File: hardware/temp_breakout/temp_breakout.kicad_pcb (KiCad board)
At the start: 2 copper layers, 45.5 x 48.5 mm, 14 parts, among them J1 Conn_01x04, J2 Conn_01x03, J3 Conn_01x03, J4 Conn_01x03, J5 Conn_01x03, J6 Conn_01x03, J7 Conn_01x03

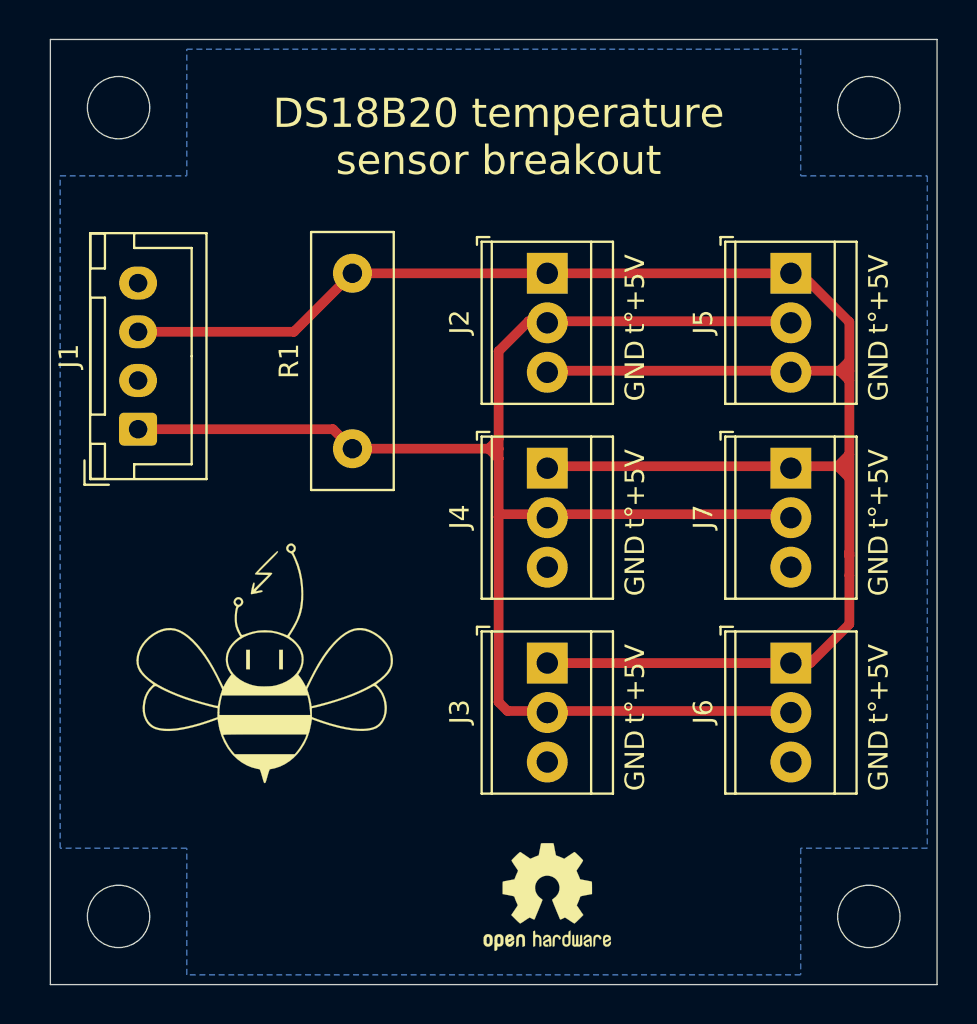
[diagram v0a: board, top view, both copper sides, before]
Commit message: fix temp breakout board bug: 5V and gnd were shorted
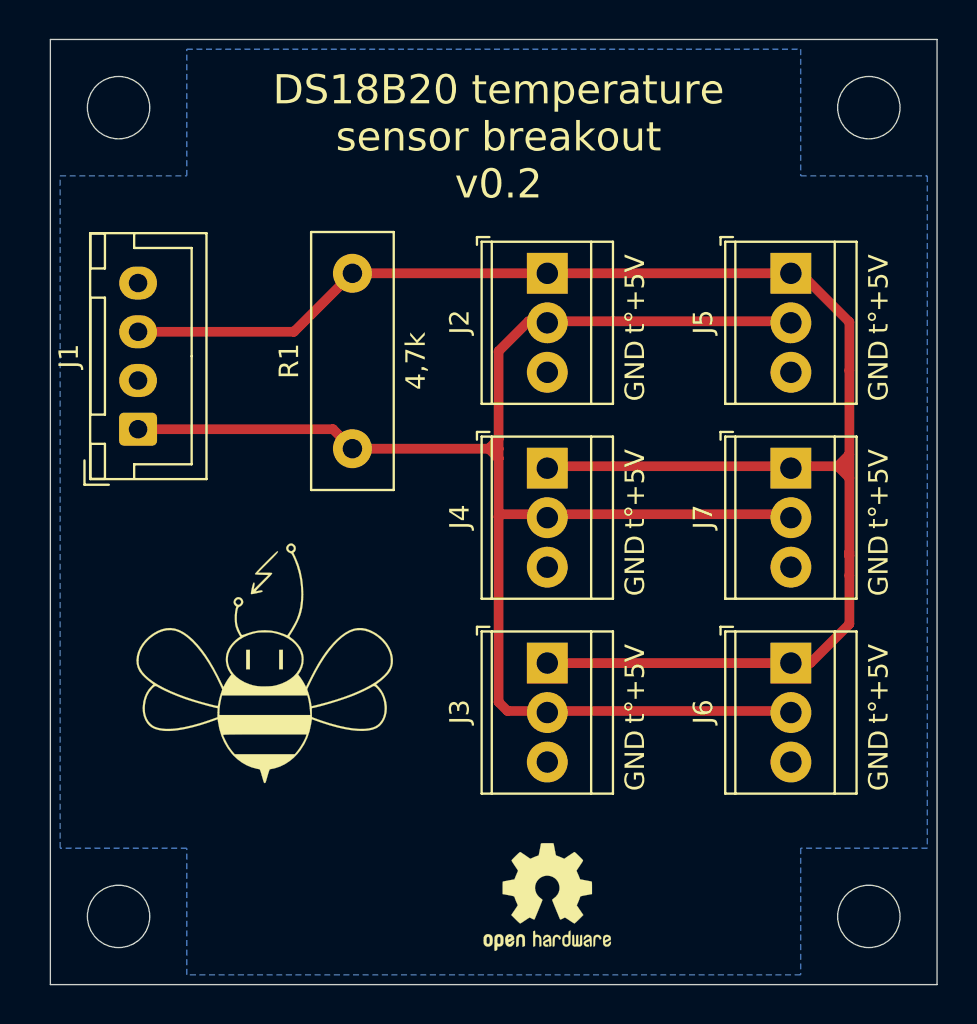
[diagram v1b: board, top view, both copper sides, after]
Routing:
- net +5V: track 104.3 -> 87.4 mm
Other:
- board text added: "DS18B20 temperature sensor breakout v0.2"
- board text removed: "DS18B20 temperature sensor breakout"
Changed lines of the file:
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@@
-(kicad_pcb (version 20171130) (host pcbnew "(5.1.7)-1")
+(kicad_pcb (version 20171130) (host pcbnew 5.1.10-88a1d61d58~90~ubuntu20.04.1)
   (general
     (thickness 1.6)
     (drawings 26)
-    (tracks 38)
+    (tracks 35)
     (zones 0)
     (modules 14)
@@
   )
   (setup
-    (last_trace_width 0.5)
+    (last_trace_width 0.25)
     (user_trace_width 0.5)
     (trace_clearance 0.2)
@@
     (visible_elements FFFFFF7F)
     (pcbplotparams
-      (layerselection 0x010fc_ffffffff)
+      (layerselection 0x3ffff_ffffffff)
       (usegerberextensions false)
       (usegerberattributes true)
@@
       (effects (font (size 1 1) (thickness 0.15)))
     )
-    (fp_text user %R (at 2.54 2 90) (layer F.Fab)
-      (effects (font (size 1 1) (thickness 0.15)))
-    )
     (fp_line (start 7.08 -3.75) (end -2 -3.75) (layer F.CrtYd) (width 0.05))
     (fp_line (start 7.08 3.75) (end 7.08 -3.75) (layer F.CrtYd) (width 0.05))
@@
     (fp_circle (center 2.54 0) (end 3.64 0) (layer F.Fab) (width 0.1))
     (fp_circle (center 0 0) (end 1.1 0) (layer F.Fab) (width 0.1))
+    (fp_text user %R (at 2.54 2 90) (layer F.Fab)
+      (effects (font (size 1 1) (thickness 0.15)))
+    )
     (pad 3 thru_hole circle (at 5.08 0 270) (size 2.1 2.1) (drill 1.1) (layers *.Cu *.Mask)
       (net 1 GND))
@@
     )
     (fp_text value Conn_01x03 (at 2.54 4.37 90) (layer F.Fab)
-      (effects (font (size 1 1) (thickness 0.15)))
-    )
-    (fp_text user %R (at 2.54 2 90) (layer F.Fab)
       (effects (font (size 1 1) (thickness 0.15)))
     )
@@
     (fp_circle (center 2.54 0) (end 3.64 0) (layer F.Fab) (width 0.1))
     (fp_circle (center 0 0) (end 1.1 0) (layer F.Fab) (width 0.1))
+    (fp_text user %R (at 2.54 2 90) (layer F.Fab)
+      (effects (font (size 1 1) (thickness 0.15)))
+    )
     (pad 3 thru_hole circle (at 5.08 0 270) (size 2.1 2.1) (drill 1.1) (layers *.Cu *.Mask)
       (net 1 GND))
@@
     )
     (fp_text value Conn_01x03 (at 2.54 4.37 90) (layer F.Fab)
-      (effects (font (size 1 1) (thickness 0.15)))
-    )
-    (fp_text user %R (at 2.54 2 90) (layer F.Fab)
       (effects (font (size 1 1) (thickness 0.15)))
     )
@@
     (fp_circle (center 2.54 0) (end 3.64 0) (layer F.Fab) (width 0.1))
     (fp_circle (center 0 0) (end 1.1 0) (layer F.Fab) (width 0.1))
+    (fp_text user %R (at 2.54 2 90) (layer F.Fab)
+      (effects (font (size 1 1) (thickness 0.15)))
+    )
     (pad 3 thru_hole circle (at 5.08 0 270) (size 2.1 2.1) (drill 1.1) (layers *.Cu *.Mask)
       (net 1 GND))
@@
     )
     (fp_text value Conn_01x03 (at 2.54 4.37 90) (layer F.Fab)
-      (effects (font (size 1 1) (thickness 0.15)))
-    )
-    (fp_text user %R (at 2.54 2 90) (layer F.Fab)
       (effects (font (size 1 1) (thickness 0.15)))
     )
@@
     (fp_circle (center 2.54 0) (end 3.64 0) (layer F.Fab) (width 0.1))
     (fp_circle (center 0 0) (end 1.1 0) (layer F.Fab) (width 0.1))
+    (fp_text user %R (at 2.54 2 90) (layer F.Fab)
+      (effects (font (size 1 1) (thickness 0.15)))
+    )
     (pad 3 thru_hole circle (at 5.08 0 270) (size 2.1 2.1) (drill 1.1) (layers *.Cu *.Mask)
       (net 1 GND))
@@
     )
     (fp_text value Conn_01x03 (at 2.54 4.37 90) (layer F.Fab)
-      (effects (font (size 1 1) (thickness 0.15)))
-    )
-    (fp_text user %R (at 2.54 2 90) (layer F.Fab)
       (effects (font (size 1 1) (thickness 0.15)))
     )
@@
     (fp_circle (center 2.54 0) (end 3.64 0) (layer F.Fab) (width 0.1))
     (fp_circle (center 0 0) (end 1.1 0) (layer F.Fab) (width 0.1))
+    (fp_text user %R (at 2.54 2 90) (layer F.Fab)
+      (effects (font (size 1 1) (thickness 0.15)))
+    )
     (pad 3 thru_hole circle (at 5.08 0 270) (size 2.1 2.1) (drill 1.1) (layers *.Cu *.Mask)
       (net 1 GND))
@@
       (effects (font (size 1 1) (thickness 0.15)))
     )
-    (fp_text value 4,7k (at 4.5 3.25 90) (layer F.Fab)
-      (effects (font (size 1 1) (thickness 0.15)))
-    )
-    (fp_text user %R (at 4.5 0 90) (layer F.Fab)
+    (fp_text value 4,7k (at 4.5 3.25 90) (layer F.SilkS)
       (effects (font (size 1 1) (thickness 0.15)))
     )
@@
     (fp_line (start 11.25 2.25) (end 11.25 -2.25) (layer F.CrtYd) (width 0.05))
     (fp_line (start 11.25 -2.25) (end -2.25 -2.25) (layer F.CrtYd) (width 0.05))
+    (fp_text user %R (at 4.5 0 90) (layer F.Fab)
+      (effects (font (size 1 1) (thickness 0.15)))
+    )
     (pad 2 thru_hole circle (at 9 0 90) (size 2 2) (drill 1) (layers *.Cu *.Mask)
       (net 2 +5V))
@@
     )
     (fp_text value Conn_01x03 (at 2.54 4.37 90) (layer F.Fab)
-      (effects (font (size 1 1) (thickness 0.15)))
-    )
-    (fp_text user %R (at 2.54 2 90) (layer F.Fab)
       (effects (font (size 1 1) (thickness 0.15)))
     )
@@
     (fp_line (start 7.08 3.75) (end 7.08 -3.75) (layer F.CrtYd) (width 0.05))
     (fp_line (start 7.08 -3.75) (end -2 -3.75) (layer F.CrtYd) (width 0.05))
+    (fp_text user %R (at 2.54 2 90) (layer F.Fab)
+      (effects (font (size 1 1) (thickness 0.15)))
+    )
     (pad 3 thru_hole circle (at 5.08 0 270) (size 2.1 2.1) (drill 1.1) (layers *.Cu *.Mask)
       (net 1 GND))
@@
     )
     (fp_text value Conn_01x04 (at 3.75 4.6 90) (layer F.Fab)
-      (effects (font (size 1 1) (thickness 0.15)))
-    )
-    (fp_text user %R (at 3.75 2.7 90) (layer F.Fab)
       (effects (font (size 1 1) (thickness 0.15)))
     )
@@
     (fp_line (start -1.6 -2.75) (end -2.85 -2.75) (layer F.SilkS) (width 0.12))
     (fp_line (start -2.85 -2.75) (end -2.85 -1.5) (layer F.SilkS) (width 0.12))
+    (fp_text user %R (at 3.75 2.7 90) (layer F.Fab)
+      (effects (font (size 1 1) (thickness 0.15)))
+    )
     (pad 4 thru_hole oval (at 7.5 0 90) (size 1.7 1.95) (drill 0.95) (layers *.Cu *.Mask)
       (net 1 GND))
@@
     (pad 1 np_thru_hole circle (at 0 0) (size 3.2 3.2) (drill 3.2) (layers *.Cu *.Mask))
   )
-  (gr_text "DS18B20 temperature\nsensor breakout" (at 135 85.5) (layer F.SilkS)
+  (gr_text "DS18B20 temperature\nsensor breakout\nv0.2" (at 135 85.5) (layer F.SilkS)
     (effects (font (size 1.5 1.5) (thickness 0.3)))
   )
@@
   )
   (gr_line (start 157.5 80.5) (end 157.5 129) (layer Edge.Cuts) (width 0.05))
-  (segment (start 152.5 97.5) (end 153 98) (width 0.5) (layer F.Cu) (net 2))
-  (segment (start 153 97) (end 152.5 97.5) (width 0.5) (layer F.Cu) (net 2))
   (segment (start 124.5 95.5) (end 127.5 92.5) (width 0.5) (layer F.Cu) (net 2))
   (segment (start 116.5 95.5) (end 124.5 95.5) (width 0.5) (layer F.Cu) (net 2))
   (segment (start 150.18 112.5) (end 137.55 112.5) (width 0.5) (layer F.Cu) (net 2))
-  (segment (start 137.5 97.5) (end 153 97.5) (width 0.5) (layer F.Cu) (net 2))
   (segment (start 153 97.5) (end 153 107) (width 0.5) (layer F.Cu) (net 2))
   (segment (start 151 112.5) (end 150.18 112.5) (width 0.5) (layer F.Cu) (net 2))

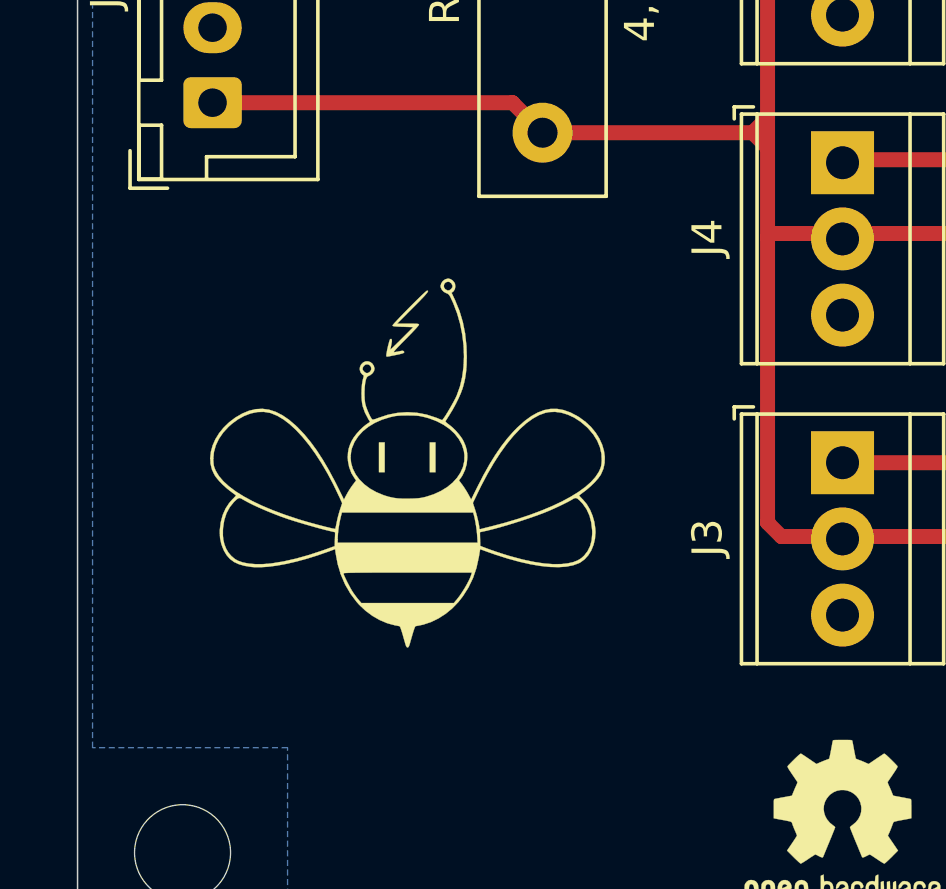
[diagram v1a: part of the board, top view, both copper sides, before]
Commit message: Apply CERN-W license
Apply CERN-W license to all boards, move the first iteration of the IR_sensor to the archive

Co-Authored-By: Andre Maia Chagas <a.maia-chagas@sussex.ac.uk>
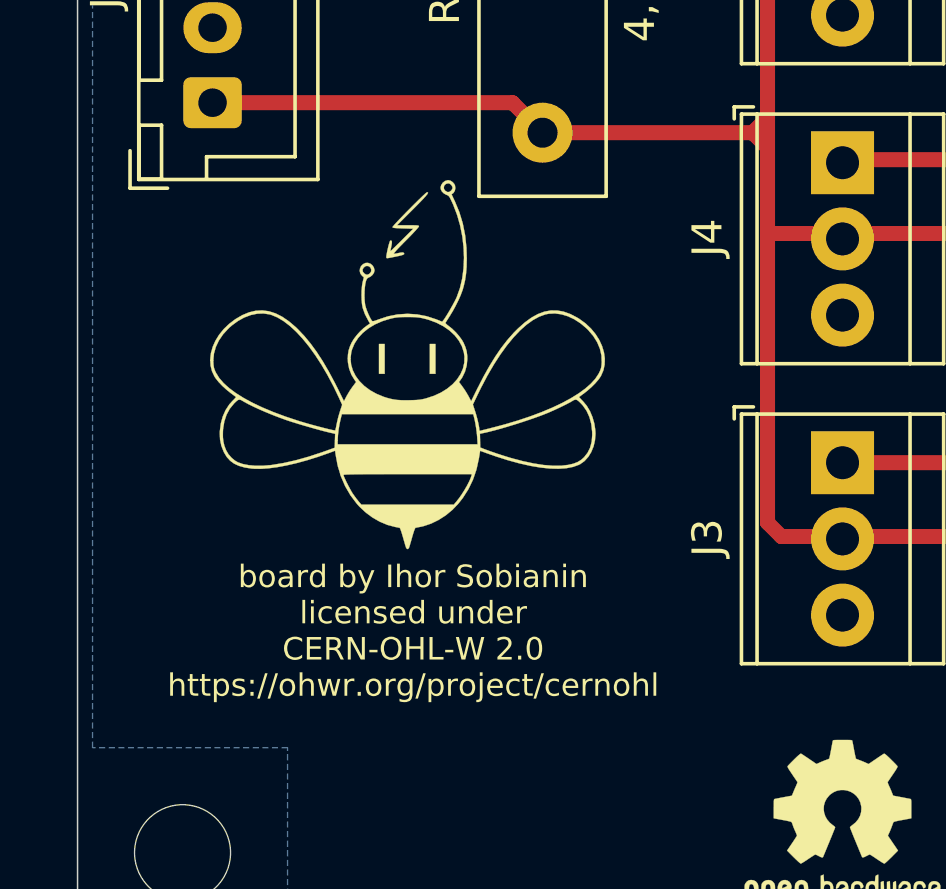
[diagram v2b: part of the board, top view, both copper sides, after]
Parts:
- moved G*** 3.28 mm to (123.0, 109.2)
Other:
- board text added: "board by Ihor Sobianin licensed under CERN-OHL-W 2.0 https://ohwr.org/project/cernohl"
